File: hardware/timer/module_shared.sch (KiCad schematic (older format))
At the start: 5 parts, among them J1 RJ45_LED_Shielded, U1 WAVGAT_CAN

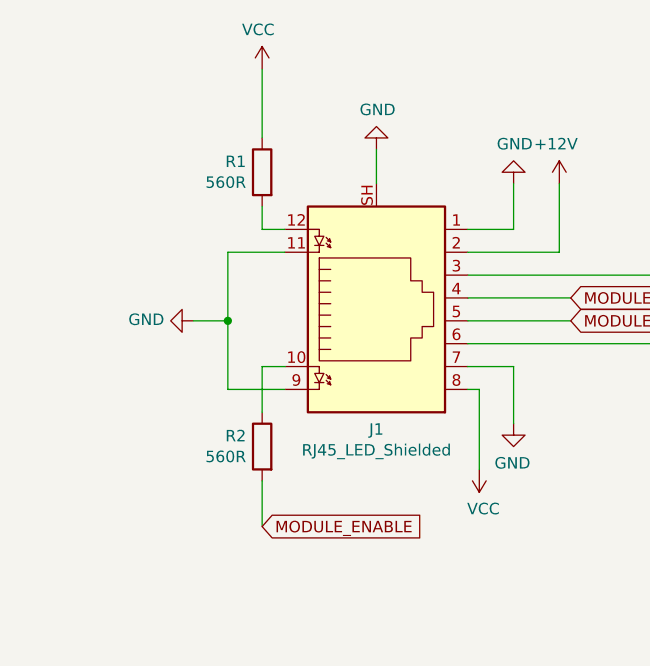
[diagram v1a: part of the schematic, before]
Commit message: Timer PCB: use non-LED RJ45, update layout, reroute
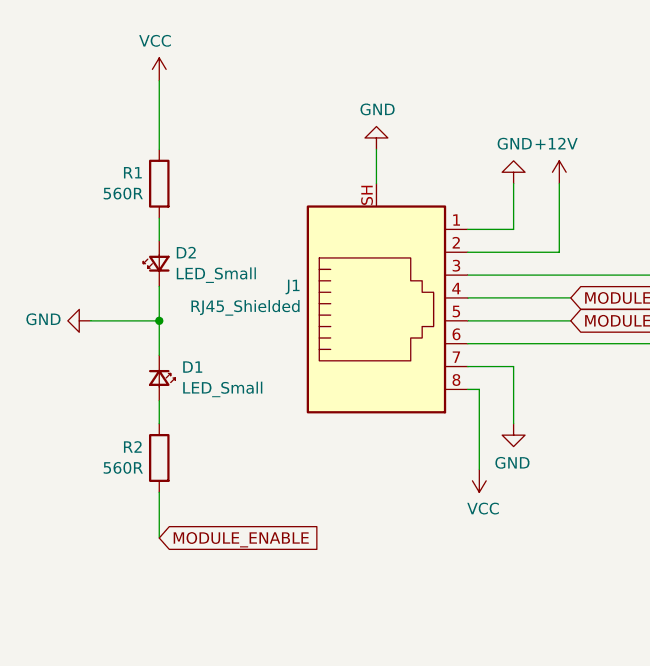
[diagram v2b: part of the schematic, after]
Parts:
- removed J1: RJ45_LED_Shielded, Connector_RJ:RJ45_Amphenol_RJHSE538X, symbol Connector:RJ45_LED_Shielded
- added D1, D2: LED_Small, LED_THT:LED_D3.0mm, symbol Device:LED_Small
- added J1: RJ45_Shielded, RJ45_5224:RJ45_5224, symbol Connector:RJ45_Shielded
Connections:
- net +12V: now also J1.2
- net GND: now also D1.1 (K), D2.1 (K), J1.1, J1.7, J1.SH
- net MODULE_ENABLE: now also J1.5
- net MODULE_READY: now also J1.4
- net VCC: now also J1.8
- net at U1.J3_1 (CAN_L): now also J1.3
- net at U1.J3_2 (CAN_H): now also J1.6
- net at R2.1: now also D1.2 (A)
- net at R1.2: now also D2.2 (A)
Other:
- moved on the sheet: R1, R2
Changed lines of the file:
@@
 Wire Wire Line
 	8750 4000 8600 4000
-Wire Wire Line
-	2150 3300 2250 3300
-Wire Wire Line
-	2150 3500 2150 3300
 $Comp
 L Device:R R?
 U 1 1 5F2CBE03
-P 2150 3650
+P 1700 3700
 AR Path="/5F2CBE03" Ref="R?"  Part="1"
 AR Path="/5EF969E2/5F2CBE03" Ref="R2"  Part="1"
 AR Path="/5EAC2475/5F2CBE03" Ref="R2"  Part="1"
-F 0 "R2" H 2220 3696 50  0000 L CNN
-F 1 "560R" H 2220 3605 50  0000 L CNN
-F 2 "Resistor_SMD:R_0603_1608Metric_Pad1.05x0.95mm_HandSolder" V 2080 3650 50  0001 C CNN
-F 3 "~" H 2150 3650 50  0001 C CNN
-	1    2150 3650
+F 0 "R2" H 1770 3746 50  0000 L CNN
+F 1 "560R" H 1770 3655 50  0000 L CNN
+F 2 "Resistor_SMD:R_0603_1608Metric_Pad1.05x0.95mm_HandSolder" V 1630 3700 50  0001 C CNN
+F 3 "~" H 1700 3700 50  0001 C CNN
+	1    1700 3700
 	-1   0    0    -1
 $EndComp
@@
 L power:VCC #PWR?
 U 1 1 5F2CBE2A
-P 2150 2000
+P 1700 2050
 AR Path="/5F2CBE2A" Ref="#PWR?"  Part="1"
 AR Path="/5EF969E2/5F2CBE2A" Ref="#PWR0109"  Part="1"
 AR Path="/5EAC2475/5F2CBE2A" Ref="#PWR0101"  Part="1"
-F 0 "#PWR0101" H 2150 1850 50  0001 C CNN
-F 1 "VCC" H 2167 2173 50  0000 C CNN
-F 2 "" H 2150 2000 50  0001 C CNN
-F 3 "" H 2150 2000 50  0001 C CNN
-	1    2150 2000
-	-1   0    0    -1
-$EndComp
-Wire Wire Line
-	2150 2700 2250 2700
-Wire Wire Line
-	2150 2600 2150 2700
+F 0 "#PWR0101" H 1700 1900 50  0001 C CNN
+F 1 "VCC" H 1717 2223 50  0000 C CNN
+F 2 "" H 1700 2050 50  0001 C CNN
+F 3 "" H 1700 2050 50  0001 C CNN
+	1    1700 2050
+	-1   0    0    -1
+$EndComp
+Wire Wire Line
+	1700 2650 1700 2750
 $Comp
 L Device:R R?
 U 1 1 5F2CBE32
-P 2150 2450
+P 1700 2500
 AR Path="/5F2CBE32" Ref="R?"  Part="1"
 AR Path="/5EF969E2/5F2CBE32" Ref="R1"  Part="1"
 AR Path="/5EAC2475/5F2CBE32" Ref="R1"  Part="1"
-F 0 "R1" H 2220 2496 50  0000 L CNN
-F 1 "560R" H 2220 2405 50  0000 L CNN
-F 2 "Resistor_SMD:R_0603_1608Metric_Pad1.05x0.95mm_HandSolder" V 2080 2450 50  0001 C CNN
-F 3 "~" H 2150 2450 50  0001 C CNN
-	1    2150 2450
-	-1   0    0    -1
-$EndComp
-Wire Wire Line
-	2000 3100 2000 3400
-Wire Wire Line
-	1850 3100 2000 3100
+F 0 "R1" H 1770 2546 50  0000 L CNN
+F 1 "560R" H 1770 2455 50  0000 L CNN
+F 2 "Resistor_SMD:R_0603_1608Metric_Pad1.05x0.95mm_HandSolder" V 1630 2500 50  0001 C CNN
+F 3 "~" H 1700 2500 50  0001 C CNN
+	1    1700 2500
+	-1   0    0    -1
+$EndComp
 $Comp
 L power:GND #PWR?
 U 1 1 5F2CBE3A
-P 1850 3100
+P 1400 3100
 AR Path="/5F2CBE3A" Ref="#PWR?"  Part="1"
 AR Path="/5EF969E2/5F2CBE3A" Ref="#PWR0110"  Part="1"
 AR Path="/5EAC2475/5F2CBE3A" Ref="#PWR0102"  Part="1"
-F 0 "#PWR0102" H 1850 2850 50  0001 C CNN
-F 1 "GND" V 1855 2972 50  0000 R CNN
-F 2 "" H 1850 3100 50  0001 C CNN
-F 3 "" H 1850 3100 50  0001 C CNN
-	1    1850 3100
+F 0 "#PWR0102" H 1400 2850 50  0001 C CNN
+F 1 "GND" V 1405 2972 50  0000 R CNN
+F 2 "" H 1400 3100 50  0001 C CNN
+F 3 "" H 1400 3100 50  0001 C CNN
+	1    1400 3100
 	0    1    -1   0
 $EndComp
-Wire Wire Line
-	2000 3400 2250 3400
-Connection ~ 2000 3100
-Wire Wire Line
-	2000 2800 2000 3100
-Wire Wire Line
-	2250 2800 2000 2800
 Wire Wire Line
 	5600 3300 6600 3300
@@
 D3
 Wire Wire Line
-	2150 4000 2150 3800
-$Comp
-L Connector:RJ45_LED_Shielded J1
-U 1 1 5F4ED7D2
-P 2650 3000
-F 0 "J1" H 2650 3575 50  0000 C CNN
-F 1 "RJ45_LED_Shielded" H 2650 3666 50  0000 C CNN
-F 2 "Connector_RJ:RJ45_Amphenol_RJHSE538X" V 2650 3025 50  0001 C CNN
-F 3 "~" V 2650 3025 50  0001 C CNN
-	1    2650 3000
-	1    0    0    1
-$EndComp
+	1700 4050 1700 3850
 $Comp
 L power:GND #PWR?
@@
 Wire Wire Line
 	2650 2350 2650 2500
-Text GLabel 2150 4000 2    50   Input ~ 0
+Text GLabel 1700 4050 2    50   Input ~ 0
 MODULE_ENABLE
 Wire Wire Line
-	2150 2000 2150 2300
+	1700 2050 1700 2350
 $Comp
 L MCU_Module:Arduino_Nano_v3.x A?
@@
 Wire Wire Line
 	8600 3700 8750 3700
+$Comp
+L Connector:RJ45_Shielded J1
+U 1 1 5F6D7F49
+P 2650 3000
+F 0 "J1" H 2320 2947 50  0000 R CNN
+F 1 "RJ45_Shielded" H 2320 3038 50  0000 R CNN
+F 2 "RJ45_5224:RJ45_5224" V 2650 3025 50  0001 C CNN
+F 3 "~" V 2650 3025 50  0001 C CNN
+	1    2650 3000
+	1    0    0    1
+$EndComp
+$Comp
+L Device:LED_Small D2
+U 1 1 5F6E139F
+P 1700 2850
+F 0 "D2" V 1746 2780 50  0000 R CNN
+F 1 "LED_Small" V 1655 2780 50  0000 R CNN
+F 2 "LED_THT:LED_D3.0mm" V 1700 2850 50  0001 C CNN
+F 3 "~" V 1700 2850 50  0001 C CNN
+	1    1700 2850
+	0    -1   -1   0
+$EndComp
+$Comp
+L Device:LED_Small D1
+U 1 1 5F6E2C58
+P 1700 3350
+F 0 "D1" V 1654 3448 50  0000 L CNN
+F 1 "LED_Small" V 1745 3448 50  0000 L CNN
+F 2 "LED_THT:LED_D3.0mm" V 1700 3350 50  0001 C CNN
+F 3 "~" V 1700 3350 50  0001 C CNN
+	1    1700 3350
+	0    1    1    0
+$EndComp
+Wire Wire Line
+	1700 3550 1700 3450
+Wire Wire Line
+	1700 3250 1700 3100
+Wire Wire Line
+	1400 3100 1700 3100
+Wire Wire Line
+	1700 2950 1700 3100
+Connection ~ 1700 3100
 $EndSCHEMATC
